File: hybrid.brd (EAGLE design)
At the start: 174 x 168.9 mm, 123 parts, among them IC1 TL071P, IC2 TL071P, IC3 LM317MABT-OUT, IC4 LM317MABT-OUT, J1 RCJ-21XXMILL, J2 NRJ3HF-1, J3 703W-00/54, Q1 BC560KINKED, Q10 BC560KINKED, Q11 BC560KINKED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

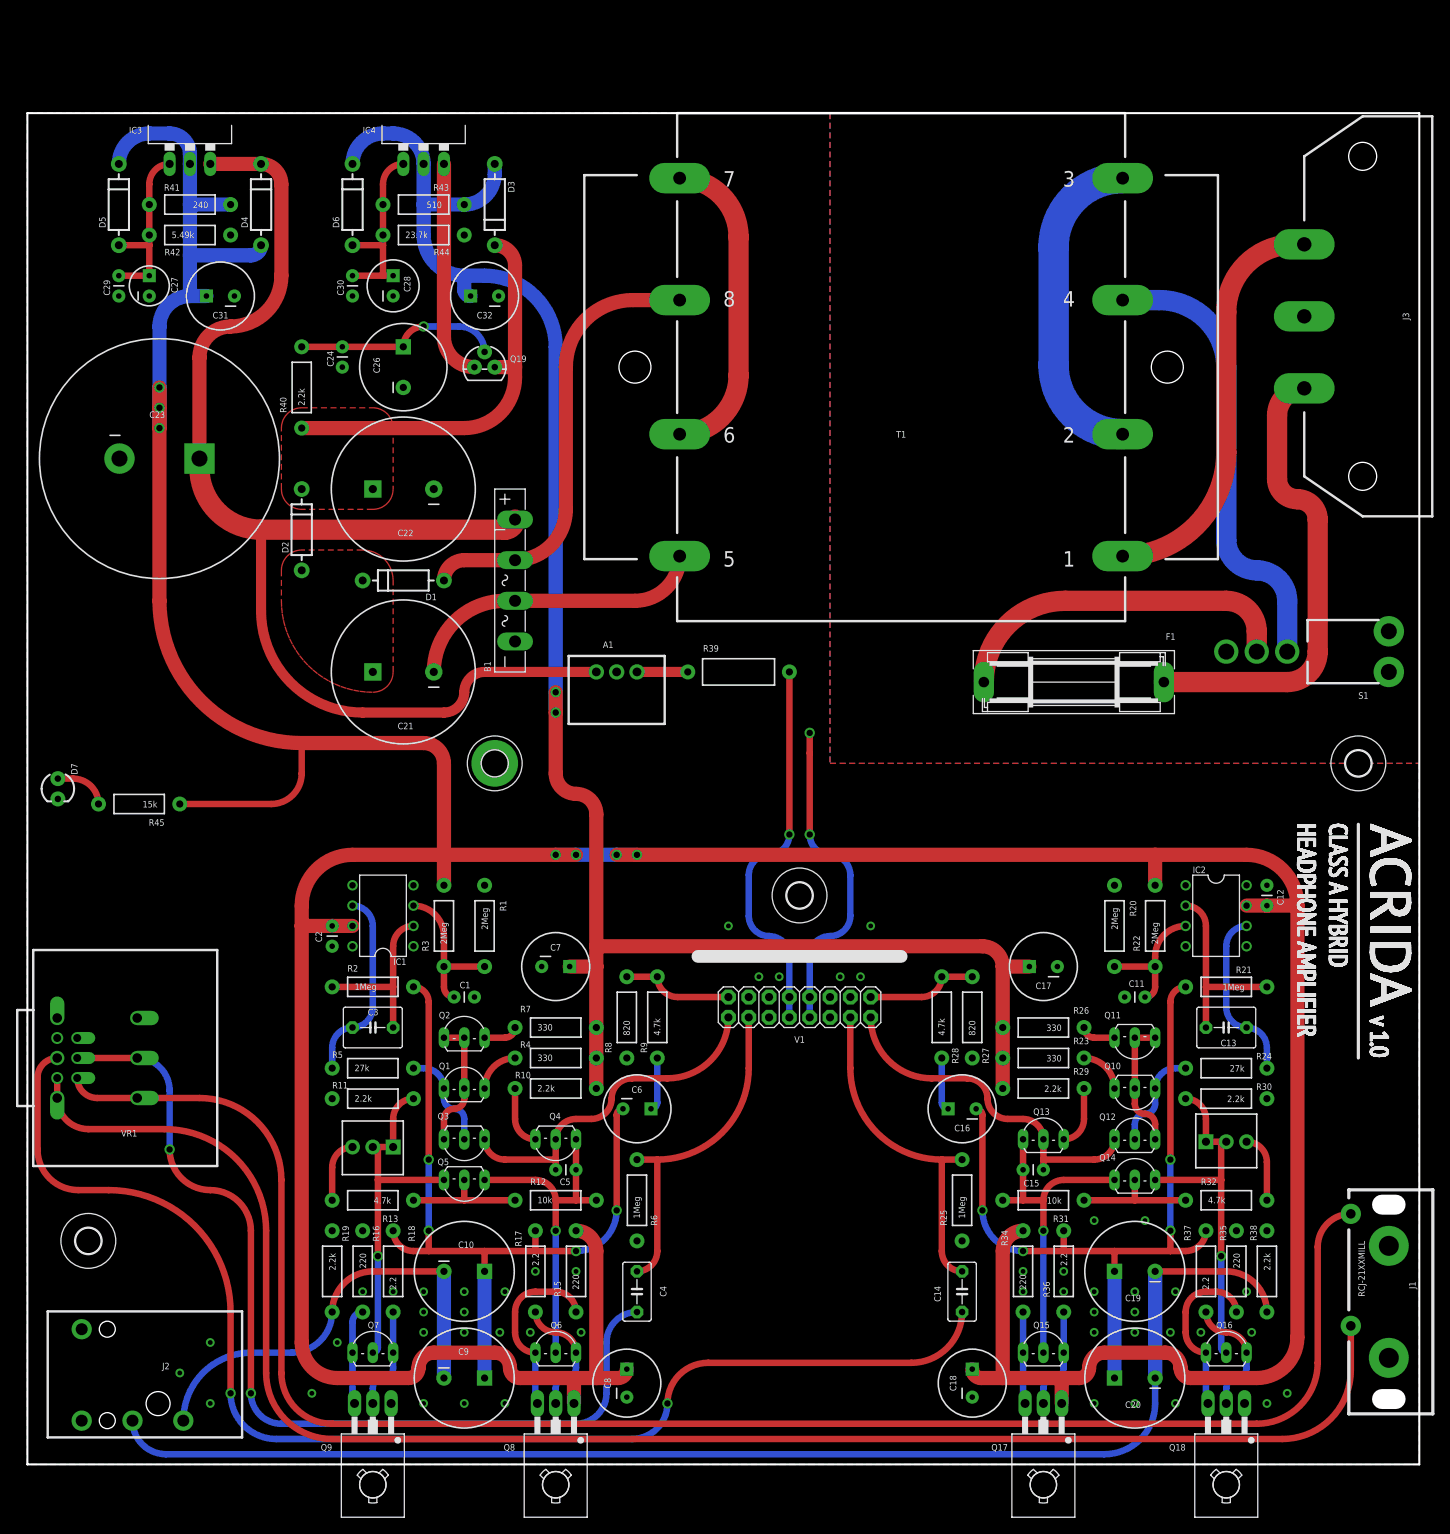
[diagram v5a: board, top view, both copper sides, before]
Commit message: Split groundplane again
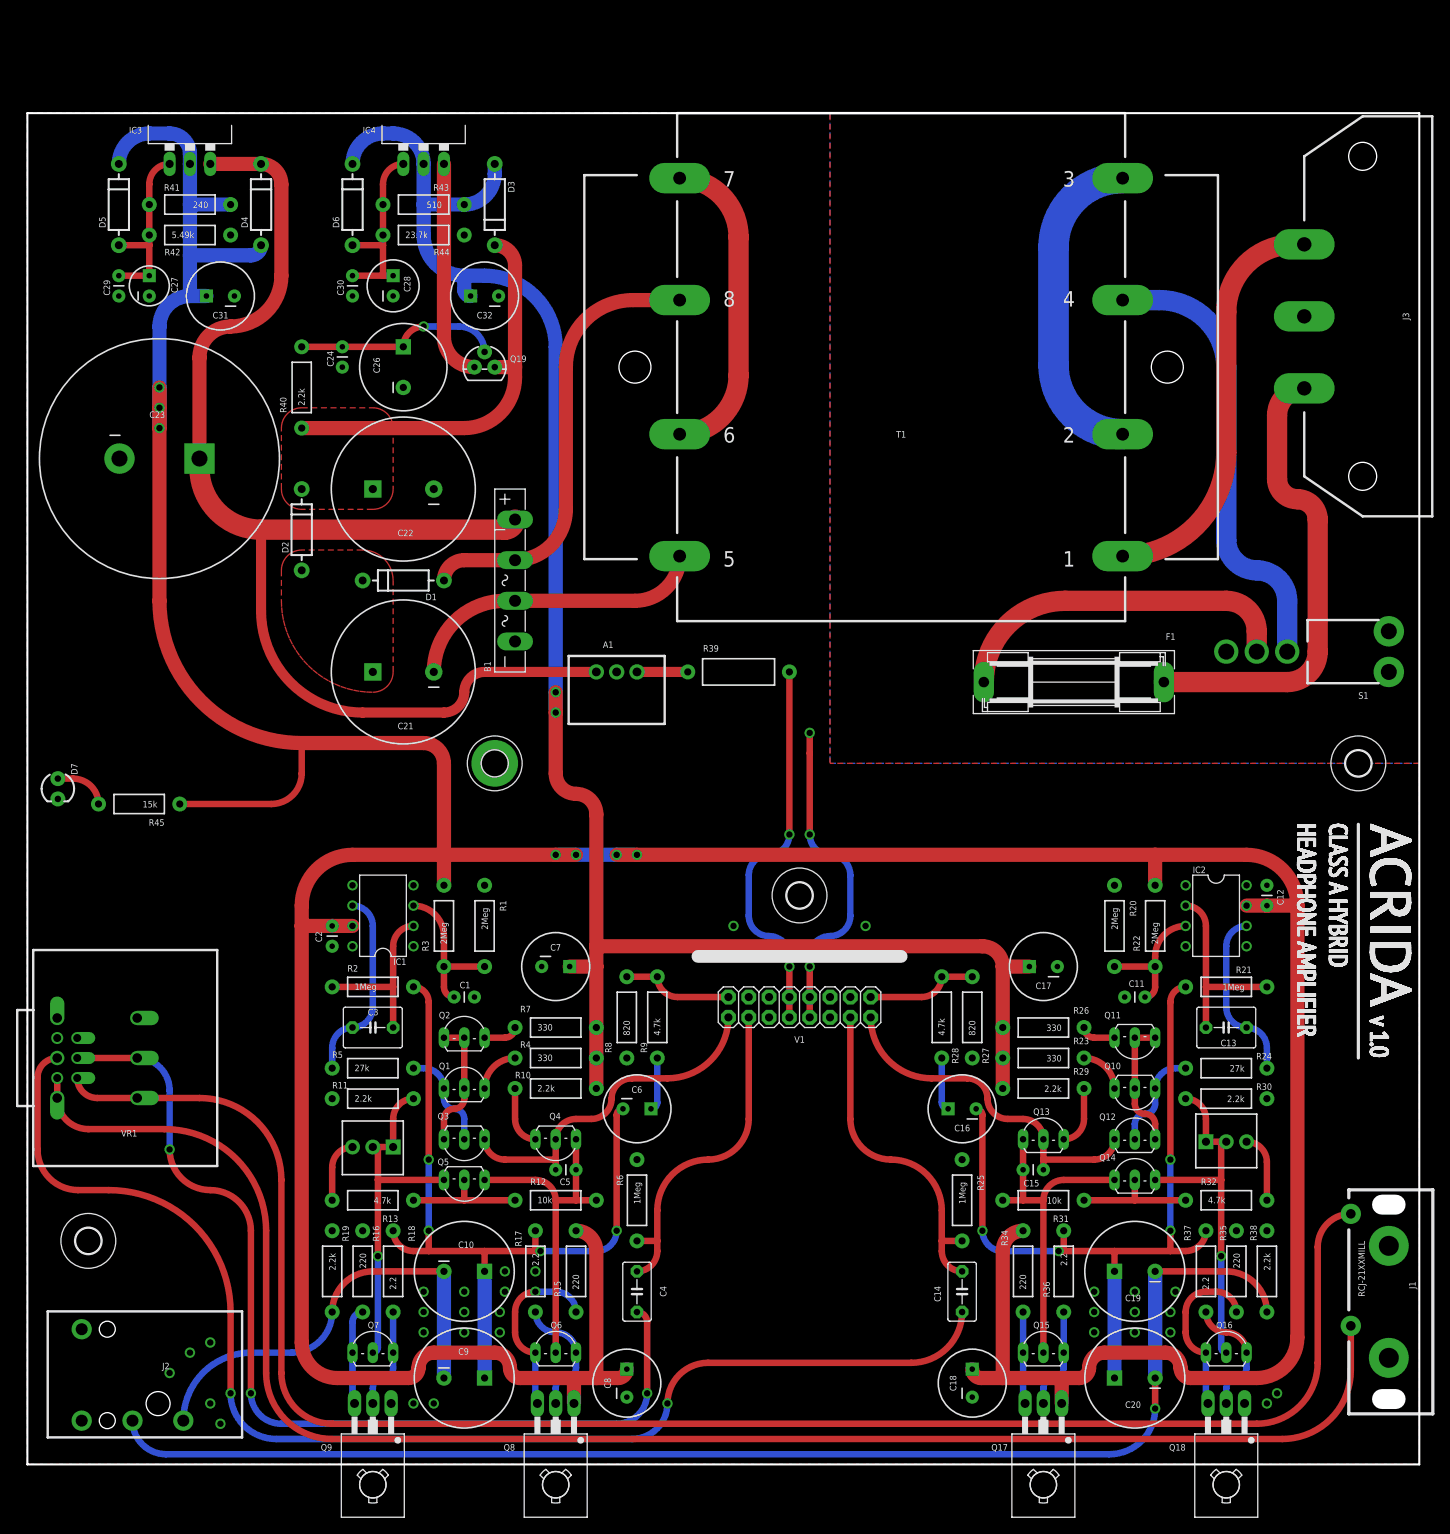
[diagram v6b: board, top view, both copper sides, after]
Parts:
- turned R25 to 270 degrees
- turned R6 to 270 degrees
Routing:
- net IN_L: track 114.6 -> 118.7 mm, vias 2 -> 3
- net FB_L: track 96.3 -> 97.8 mm
- net FB_R: track 96.3 -> 97.8 mm
- net OUT_R: track 164.8 -> 165.2 mm, vias 0 -> 1
- net N$7: vias 1 -> 0
- net N$21: vias 1 -> 0
- net N$14: vias 0 -> 1
- net GND: vias 51 -> 32
- net FGND: vias 1 -> 2
- net +6.3FIL: vias 1 -> 2
